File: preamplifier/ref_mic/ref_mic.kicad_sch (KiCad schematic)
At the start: 28 parts, among them J1 XLR3, U1 OPA1611

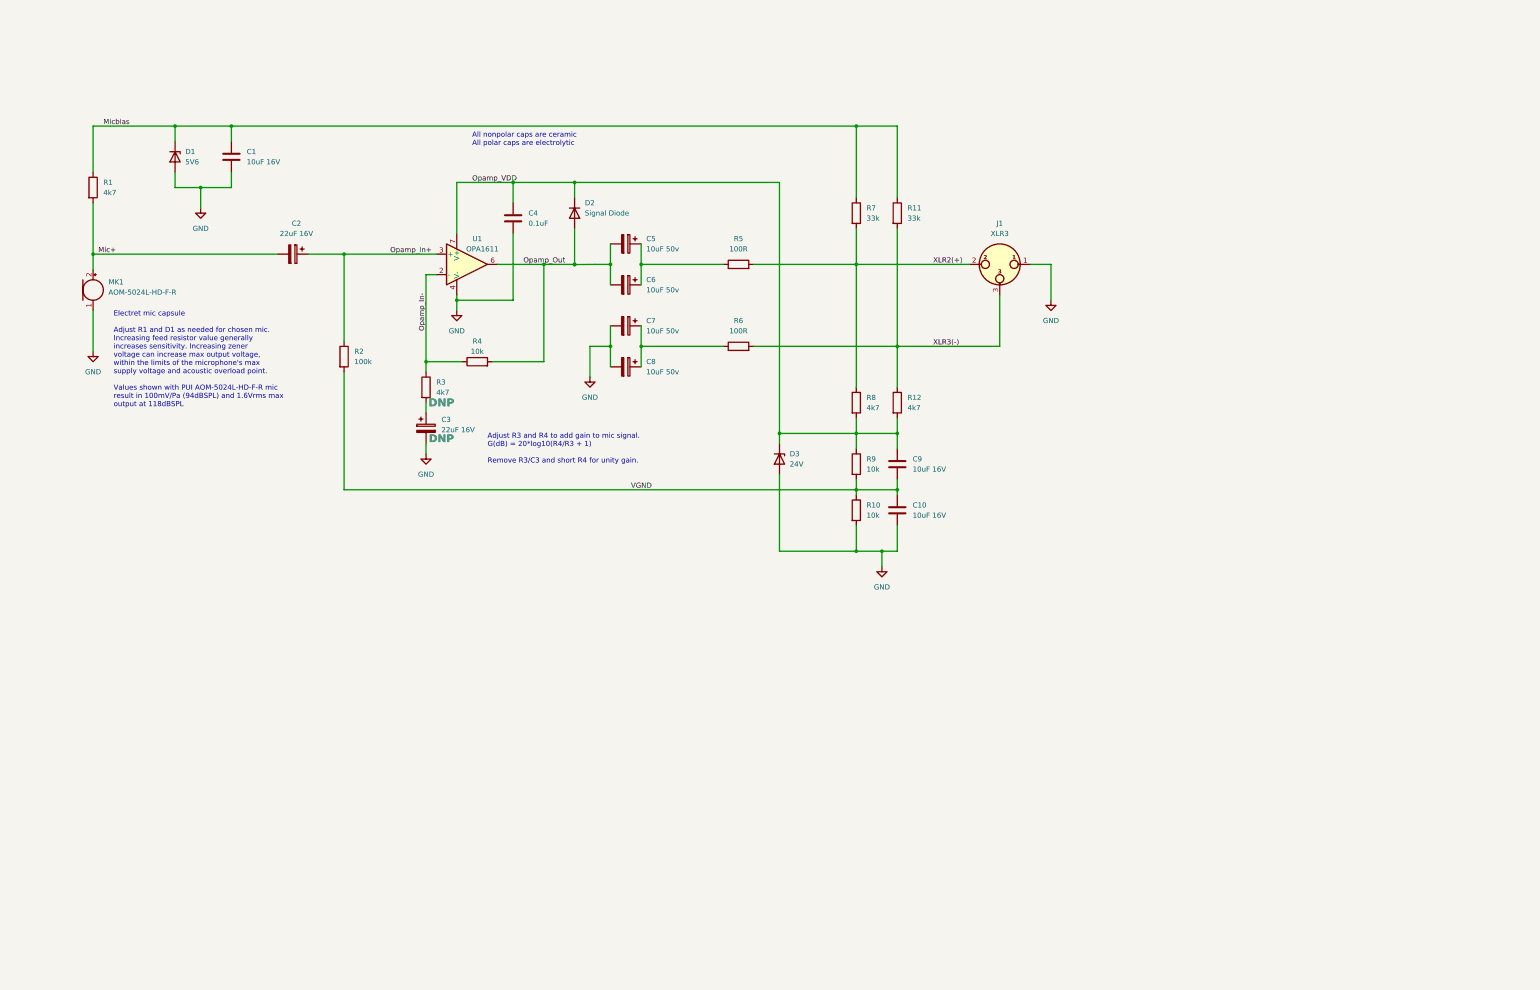
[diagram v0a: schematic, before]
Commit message: Initial v2 schematic, including high frequency correction filter for specified mic, library for slide switch. Update project to KiCAD 9.0 and change DNPs to use built in DNP feature.
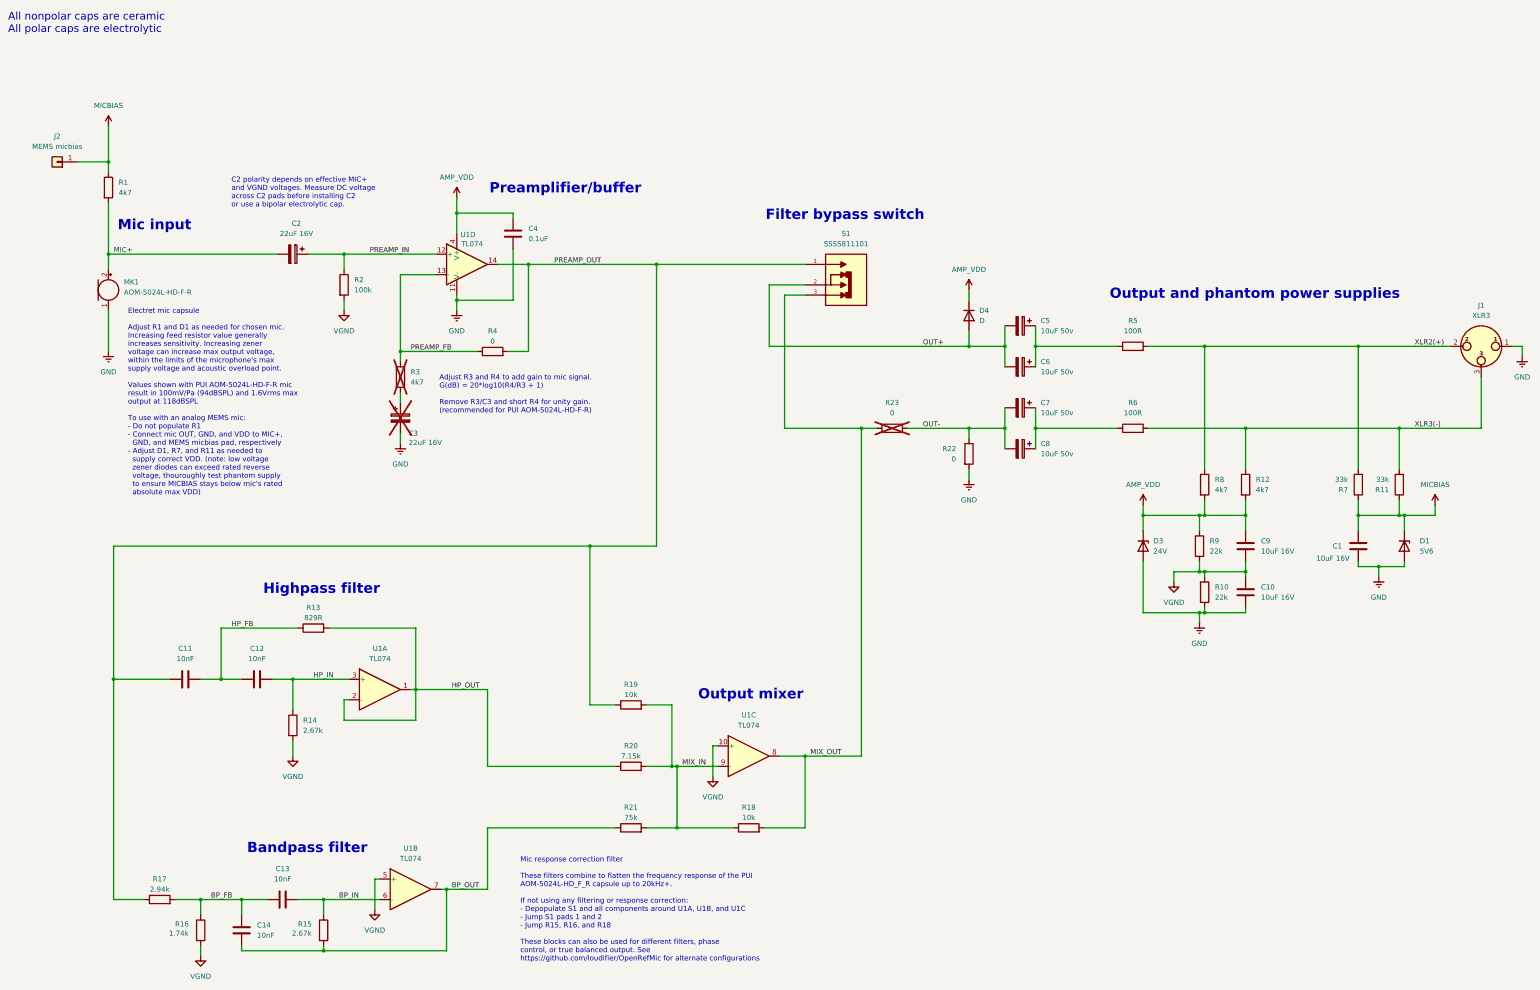
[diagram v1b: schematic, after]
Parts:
- removed D2: Signal Diode, Package_TO_SOT_SMD:SOT-23_Handsoldering, symbol Simulation_SPICE:DIODE
- removed U1: OPA1611, Package_SO:SOIC-8_3.9x4.9mm_P1.27mm, symbol Simulation_SPICE:OPAMP
- added C11, C12, C13, C14: 10nF, Capacitor_SMD:C_0805_2012Metric_Pad1.18x1.45mm_HandSolder, symbol Device:C
- added D4: D, symbol Device:D
- added J2: MEMS micbias, symbol Connector_Generic:Conn_01x01
- added R13: 829R, Resistor_SMD:R_0603_1608Metric_Pad0.98x0.95mm_HandSolder, symbol Device:R
- added R14, R15: 2.67k, Resistor_SMD:R_0603_1608Metric_Pad0.98x0.95mm_HandSolder, symbol Device:R
- added R16: 1.74k, Resistor_SMD:R_0603_1608Metric_Pad0.98x0.95mm_HandSolder, symbol Device:R
- added R17: 2.94k, Resistor_SMD:R_0603_1608Metric_Pad0.98x0.95mm_HandSolder, symbol Device:R
- added R18, R19: 10k, Resistor_SMD:R_0603_1608Metric_Pad0.98x0.95mm_HandSolder, symbol Device:R
- added R20: 7.15k, Resistor_SMD:R_0603_1608Metric_Pad0.98x0.95mm_HandSolder, symbol Device:R
- added R21: 75k, Resistor_SMD:R_0603_1608Metric_Pad0.98x0.95mm_HandSolder, symbol Device:R
- added R22, R23: 0, Resistor_SMD:R_0603_1608Metric_Pad0.98x0.95mm_HandSolder, symbol Device:R
- added S1: SSSS811101, SSSS811101:SW_SSSS811101, symbol SSSS811101:SSSS811101
- added U1, U2: TL074, symbol Amplifier_Operational:TL074
- C3, R3: DNP DNP -> (none); now not fitted
- R10, R9: value 10k -> 22k
- R4: value 10k -> 0
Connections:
- net GND: now also R22.2, U2.11 (V-); no longer C7.2, C8.2
- net VGND: now also R14.2, R16.2, U1.10 (+), U1.5 (+)
- net Mic+ renamed MIC+
- net Micbias renamed MICBIAS
- net MICBIAS: now also J2.1 (Pin_1)
- net Opamp_In+ renamed PREAMP_IN
- net PREAMP_IN: now also U1.12 (+)
- net Opamp_In- renamed PREAMP_FB
- net PREAMP_FB: now also U1.13 (-)
- net Opamp_Out renamed OUT+
- net OUT+: now also D4.2 (A), S1.2; no longer R4.2
- net Opamp_VDD renamed AMP_VDD
- net AMP_VDD: now also D4.1 (K), U2.4 (V+)
- new net BP_FB: C13.1, C14.2, R16.1, R17.2
- new net BP_IN: C13.2, R15.1, U1.6 (-)
- new net BP_OUT: C14.1, R15.2, R21.1, U1.7
- new net HP_FB: C11.2, C12.1, R13.1
- new net HP_IN: C12.2, R14.1, U1.3 (+)
- new net HP_OUT: R13.2, R20.1, U1.1, U1.2 (-)
- new net MIX_IN: R18.1, R19.2, R20.2, R21.2, U1.9 (-)
- new net MIX_OUT: R18.2, R23.1, S1.3, U1.8
- new net OUT-: C7.2, C8.2, R22.1, R23.2
- new net PREAMP_OUT: C11.1, R17.1, R19.1, R4.2, S1.1, U1.14
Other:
- note added: "Adjust R3 and R4 to add gain to mic signal. G(dB) = 20*log10(R4/R3 + 1) Remove R3/C3 and short R4 for unity gain. (recommended for PUI AOM-5024L-HD-F-R)"
- note added: "Bandpass filter"
- note added: "C2 polarity depends on effective MIC+ and VGND voltages. Measure DC voltage across C2 pads before installing C2 or use a bipolar electrolytic cap."
- note added: "Electret mic capsule Adjust R1 and D1 as needed for chosen mic. Increasing feed resistor value generally increases sensitivity. Increasing zener voltage can increase max output voltage, within the limits of the microphone's max supply voltage and acoustic overload point. Values shown with PUI AOM-5024L-HD-F-R mic result in 100mV/Pa (94dBSPL) and 1.6Vrms max output at 118dBSPL To use with an analo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"
- note added: "Filter bypass switch"
- note added: "Highpass filter"
- note added: "Mic input"
- note added: "Mic response correction filter These filters combine to flatten the frequency response of the PUI AOM-5024L-HD_F_R capsule up to 20kHz+. If not using any filtering or response correction: - Depopulate S1 and all components around U1A, U1B, and U1C - Jump S1 pads 1 and 2 - Jump R15, R16, and R18 These blocks can also be used for different filters, phase control, or true balanced output. See https: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"
- note added: "Output and phantom power supplies"
- note added: "Output mixer"
- note added: "Preamplifier/buffer"
- note removed: "Adjust R3 and R4 to add gain to mic signal. G(dB) = 20*log10(R4/R3 + 1) Remove R3/C3 and short R4 for unity gain."
- note removed: "Electret mic capsule Adjust R1 and D1 as needed for chosen mic. Increasing feed resistor value generally increases sensitivity. Increasing zener voltage can increase max output voltage, within the limits of the microphone's max supply voltage and acoustic overload point. Values shown with PUI AOM-5024L-HD-F-R mic result in 100mV/Pa (94dBSPL) and 1.6Vrms max output at 118dBSPL"
- moved on the sheet: C1, C10, C4, C5, C6, C7, C8, C9, D1, D3, J1, MK1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

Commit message: Bulk of v2 updates, before assembly and testing new design - KiCAD project - gerber outputs - schematic PDF - mechanical design (Fusion project, STEP assembly, STL outputs)
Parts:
- removed C6, C8: 10uF 50v, Capacitor_SMD:CP_Elec_6.3x5.4_Nichicon, symbol Device:C_Polarized
- added C1: 4.7uF 35V, Capacitor_SMD:CP_Elec_4x4.5, symbol Device:C_Polarized
- C10: renamed from C7; footprint Capacitor_SMD:CP_Elec_6.3x5.4_Nichicon -> Capacitor_SMD:CP_Elec_6.3x4.5; DigiKey_Part_Number (none) -> UZG1H100MCL1GB; LCSC_Part_Number (none) -> Honor Elec GVS1H100M0604
- C11: renamed from C9; footprint Capacitor_SMD:C_0805_2012Metric_Pad1.18x1.45mm_HandSolder -> Capacitor_SMD:C_1206_3216Metric; DigiKey_Part_Number (none) -> CL31B106KOHNNNE; LCSC_Part_Number (none) -> Samsung Electro-Mechanics CL31B106KOHNNNE; Size (none) -> 1206
- C12: renamed from C10; footprint Capacitor_SMD:C_0805_2012Metric_Pad1.18x1.45mm_HandSolder -> Capacitor_SMD:C_1206_3216Metric; DigiKey_Part_Number (none) -> CL31B106KOHNNNE; LCSC_Part_Number (none) -> Samsung Electro-Mechanics CL31B106KOHNNNE
- C13: renamed from C1; footprint Capacitor_SMD:C_0805_2012Metric_Pad1.18x1.45mm_HandSolder -> Capacitor_SMD:C_1206_3216Metric; DigiKey_Part_Number (none) -> CL31B106KOHNNNE; LCSC_Part_Number (none) -> Samsung Electro-Mechanics CL31B106KOHNNNE
- C2: value 22uF 16V -> 4.7uF 35V; footprint Capacitor_SMD:CP_Elec_5x5.4 -> Capacitor_SMD:CP_Elec_4x4.5; DigiKey_Part_Number (none) -> UZR1V4R7MCL1GB; LCSC_Part_Number (none) -> Lelon VSS100M1CTR-0404
- C3: renamed from C11; footprint Capacitor_SMD:C_0805_2012Metric_Pad1.18x1.45mm_HandSolder -> Capacitor_SMD:C_0402_1005Metric; DigiKey_Part_Number (none) -> CC0402KRX7R9BB103; LCSC_Part_Number (none) -> YAGEO CC0402KRX7R9BB103
- C4: renamed from C12; footprint Capacitor_SMD:C_0805_2012Metric_Pad1.18x1.45mm_HandSolder -> Capacitor_SMD:C_0402_1005Metric; DigiKey_Part_Number (none) -> CC0402KRX7R9BB103; LCSC_Part_Number (none) -> YAGEO CC0402KRX7R9BB103
- C5: renamed from C14; footprint Capacitor_SMD:C_0805_2012Metric_Pad1.18x1.45mm_HandSolder -> Capacitor_SMD:C_0402_1005Metric; DigiKey_Part_Number (none) -> CC0402KRX7R9BB103; LCSC_Part_Number (none) -> YAGEO CC0402KRX7R9BB103
- C6: renamed from C13; footprint Capacitor_SMD:C_0805_2012Metric_Pad1.18x1.45mm_HandSolder -> Capacitor_SMD:C_0402_1005Metric; DigiKey_Part_Number (none) -> CC0402KRX7R9BB103; LCSC_Part_Number (none) -> YAGEO CC0402KRX7R9BB103
- C7: renamed from C3; value 22uF 16V -> 10uF 16V; footprint Capacitor_SMD:CP_Elec_5x5.4 -> Capacitor_SMD:CP_Elec_4x4.5; DigiKey_Part_Number (none) -> UZG1C100MCL1GB; LCSC_Part_Number (none) -> Lelon VSS100M1CTR-0404; now in the parts list
- C8: renamed from C4; footprint Capacitor_SMD:C_0603_1608Metric_Pad1.08x0.95mm_HandSolder -> Capacitor_SMD:C_0402_1005Metric; DigiKey_Part_Number (none) -> CC0402KRX5R9BB104; LCSC_Part_Number (none) -> YAGEO CC0402KRX5R9BB104
- C9: renamed from C5; footprint Capacitor_SMD:CP_Elec_6.3x5.4_Nichicon -> Capacitor_SMD:CP_Elec_6.3x4.5; DigiKey_Part_Number (none) -> UZG1H100MCL1GB; LCSC_Part_Number (none) -> Honor Elec GVS1H100M0604
- D1: renamed from D4; value D -> 1N4148; footprint (none) -> Diode_SMD:D_SOD-523; DigiKey_Part_Number (none) -> 1N4148X-TP; LCSC_Part_Number (none) -> MCC 1N4148X-TP
- D2: renamed from D3; footprint Package_TO_SOT_SMD:SOT-23_Handsoldering -> Diode_SMD:D_SOD-523; DigiKey_Part_Number (none) -> BZT585B24T-7; LCSC_Part_Number (none) -> Diodes Incorporated BZT585B24T-7
- D3: renamed from D1; footprint Package_TO_SOT_SMD:SC-59_Handsoldering -> Diode_SMD:D_SOD-523; DigiKey_Part_Number (none) -> BZT52C5V6T-7; LCSC_Part_Number (none) -> Diodes Incorporated BZT52C5V6T-7
- J1: renamed from J2; footprint (none) -> Connector_PinHeader_2.54mm:PinHeader_1x01_P2.54mm_Vertical; now left out of the parts list
- J2: renamed from J1; value XLR3 -> Mini XLR Male; footprint Connector_PinHeader_2.54mm:PinHeader_1x03_P2.54mm_Vertical -> OpenRefMic:Switchcraft_T3BM_edgemount; DigiKey_Part_Number (none) -> TB3M; LCSC_Part_Number (none) -> Switchcraft TB3M (not normally stocked)
- MK1: footprint Connector_PinHeader_2.54mm:PinHeader_1x02_P2.54mm_Vertical -> Connector_PinSocket_2.54mm:PinSocket_1x02_P2.54mm_Horizontal; DigiKey_Part_Number (none) -> AOM-5024L-HD-F-R; LCSC_Part_Number (none) -> PUI Audio, Inc. AOM-5024L-HD-F-R (not normally stocked)
- R1: footprint Resistor_SMD:R_0603_1608Metric_Pad0.98x0.95mm_HandSolder -> Resistor_SMD:R_0402_1005Metric; DigiKey_Part_Number (none) -> RC0402FR-074K7L; LCSC_Part_Number (none) -> YAGEO RC0402FR-074K7L
- R10: renamed from R19; footprint Resistor_SMD:R_0603_1608Metric_Pad0.98x0.95mm_HandSolder -> Resistor_SMD:R_0402_1005Metric; DigiKey_Part_Number (none) -> RC0402FR-0710KL; LCSC_Part_Number (none) -> YAGEO RC0402FR-0710KL
- R11: renamed from R20; footprint Resistor_SMD:R_0603_1608Metric_Pad0.98x0.95mm_HandSolder -> Resistor_SMD:R_0402_1005Metric; DigiKey_Part_Number (none) -> RC0402FR-077K15L; LCSC_Part_Number (none) -> YAGEO RC0402FR-077K15L
- R12: renamed from R21; footprint Resistor_SMD:R_0603_1608Metric_Pad0.98x0.95mm_HandSolder -> Resistor_SMD:R_0402_1005Metric; DigiKey_Part_Number (none) -> RC0402FR-1375KL; LCSC_Part_Number (none) -> YAGEO RC0402FR-1375KL
- R13: renamed from R18; footprint Resistor_SMD:R_0603_1608Metric_Pad0.98x0.95mm_HandSolder -> Resistor_SMD:R_0402_1005Metric; DigiKey_Part_Number (none) -> RC0402FR-0710KL; LCSC_Part_Number (none) -> YAGEO RC0402FR-0710KL
- R14: renamed from R23; footprint Resistor_SMD:R_0603_1608Metric_Pad0.98x0.95mm_HandSolder -> Resistor_SMD:R_0402_1005Metric; DigiKey_Part_Number (none) -> RC0402JR-070RL; LCSC_Part_Number (none) -> YAGEO RC0402JR-070RL
- R15: renamed from R22; footprint Resistor_SMD:R_0603_1608Metric_Pad0.98x0.95mm_HandSolder -> Resistor_SMD:R_0402_1005Metric; DigiKey_Part_Number (none) -> RC0402JR-070RL; LCSC_Part_Number (none) -> YAGEO RC0402JR-070RL
- R16: renamed from R5; footprint Resistor_SMD:R_0603_1608Metric_Pad0.98x0.95mm_HandSolder -> Resistor_SMD:R_0402_1005Metric; DigiKey_Part_Number (none) -> RC0402FR-07100RL; LCSC_Part_Number (none) -> YAGEO RC0402FR-07100RL
- R17: renamed from R6; footprint Resistor_SMD:R_0603_1608Metric_Pad0.98x0.95mm_HandSolder -> Resistor_SMD:R_0402_1005Metric; DigiKey_Part_Number (none) -> RC0402FR-07100RL; LCSC_Part_Number (none) -> YAGEO RC0402FR-07100RL
- R18: renamed from R9; footprint Resistor_SMD:R_0603_1608Metric_Pad0.98x0.95mm_HandSolder -> Resistor_SMD:R_0402_1005Metric; DigiKey_Part_Number (none) -> RC0402FR-0722KL; LCSC_Part_Number (none) -> YAGEO RC0402FR-0722KL
- R19: renamed from R8; footprint Resistor_SMD:R_0603_1608Metric_Pad0.98x0.95mm_HandSolder -> Resistor_SMD:R_0402_1005Metric; DigiKey_Part_Number (none) -> RC0402FR-074K7L; LCSC_Part_Number (none) -> YAGEO RC0402FR-074K7L
- R2: renamed from R17; footprint Resistor_SMD:R_0603_1608Metric_Pad0.98x0.95mm_HandSolder -> Resistor_SMD:R_0402_1005Metric; DigiKey_Part_Number (none) -> RC0402FR-072K94L; LCSC_Part_Number (none) -> YAGEO RC0402FR-072K94L
- R20: renamed from R10; footprint Resistor_SMD:R_0603_1608Metric_Pad0.98x0.95mm_HandSolder -> Resistor_SMD:R_0402_1005Metric; DigiKey_Part_Number (none) -> RC0402FR-0722KL; LCSC_Part_Number (none) -> YAGEO RC0402FR-0722KL
- R21: renamed from R12; footprint Resistor_SMD:R_0603_1608Metric_Pad0.98x0.95mm_HandSolder -> Resistor_SMD:R_0402_1005Metric; DigiKey_Part_Number (none) -> RC0402FR-074K7L; LCSC_Part_Number (none) -> YAGEO RC0402FR-074K7L
- R22: renamed from R7; footprint Resistor_SMD:R_0603_1608Metric_Pad0.98x0.95mm_HandSolder -> Resistor_SMD:R_0402_1005Metric; DigiKey_Part_Number (none) -> RC0402FR-0733KL; LCSC_Part_Number (none) -> YAGEO RC0402FR-0733KL
- R23: renamed from R11; footprint Resistor_SMD:R_0603_1608Metric_Pad0.98x0.95mm_HandSolder -> Resistor_SMD:R_0402_1005Metric; DigiKey_Part_Number (none) -> RC0402FR-0733KL; LCSC_Part_Number (none) -> YAGEO RC0402FR-0733KL
- R3: renamed from R16; footprint Resistor_SMD:R_0603_1608Metric_Pad0.98x0.95mm_HandSolder -> Resistor_SMD:R_0402_1005Metric; DigiKey_Part_Number (none) -> RC0402FR-071K74L; LCSC_Part_Number (none) -> YAGEO RC0402FR-071K74L
- R4: renamed from R14; footprint Resistor_SMD:R_0603_1608Metric_Pad0.98x0.95mm_HandSolder -> Resistor_SMD:R_0402_1005Metric; DigiKey_Part_Number (none) -> RC0402FR-072K67L; LCSC_Part_Number (none) -> YAGEO RC0402FR-072K67L
- R5: renamed from R13; value 829R -> 825R; footprint Resistor_SMD:R_0603_1608Metric_Pad0.98x0.95mm_HandSolder -> Resistor_SMD:R_0402_1005Metric; DigiKey_Part_Number (none) -> RC0402FR-07825RL; LCSC_Part_Number (none) -> YAGEO RC0402FR-07825RL
- R6: renamed from R15; footprint Resistor_SMD:R_0603_1608Metric_Pad0.98x0.95mm_HandSolder -> Resistor_SMD:R_0402_1005Metric; DigiKey_Part_Number (none) -> RC0402FR-072K67L; LCSC_Part_Number (none) -> YAGEO RC0402FR-072K67L
- R7: renamed from R2; footprint Resistor_SMD:R_0603_1608Metric_Pad0.98x0.95mm_HandSolder -> Resistor_SMD:R_0402_1005Metric; DigiKey_Part_Number (none) -> RC0402FR-07100KL; LCSC_Part_Number (none) -> YAGEO RC0402FR-07100KL
- R8: renamed from R3; footprint Resistor_SMD:R_0603_1608Metric_Pad0.98x0.95mm_HandSolder -> Resistor_SMD:R_0402_1005Metric; DigiKey_Part_Number (none) -> RC0402FR-074K7L; LCSC_Part_Number (none) -> YAGEO RC0402FR-074K7L; now in the parts list
- R9: renamed from R4; footprint Resistor_SMD:R_0603_1608Metric_Pad0.98x0.95mm_HandSolder -> Resistor_SMD:R_0402_1005Metric; DigiKey_Part_Number (none) -> RC0402JR-070RL; LCSC_Part_Number (none) -> YAGEO RC0402JR-070RL
- S1: value SSSS811101 -> CL-SB-12B-01T; footprint SSSS811101:SW_SSSS811101 -> OpenRefMic:CL-SB-12B-01_NDC; symbol SSSS811101:SSSS811101 -> Switch:SW_SPDT; Check_prices https://www.snapeda.com/parts/SSSS811101/ALPS/view-part/?re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 -> (none); Description_1 Switch Slide SP Side Slide 0.3A 5VDC 10000Cycles Gull Wing 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 -> (none); DigiKey_Part_Number 4809-SSSS811101TR-ND -> CL-SB-12B-01T; LCSC_Part_Number (none) -> Nidec CL-SB-12B-01T; MANUFACTURER ALPS -> (none); MAXIMUM_PACKAGE_HEIGHT 1.60 mm -> (none); MF ALPS -> (none); MP SSSS811101 -> (none); PARTREV N/A -> (none); Package None -> (none); STANDARD Manufacturer Recommendations -> (none); SnapEDA_Link https://www.snapeda.com/parts/SSSS811101/ALPS/view-part/?re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 -> (none)
- U1: renamed from U2; value TL074 -> OPA1664; footprint (none) -> Package_SO:SO-14_3.9x8.65mm_P1.27mm; DigiKey_Part_Number (none) -> OPA1664AIDR; LCSC_Part_Number (none) -> TI OPA1664AID
- U1: value TL074 -> OPA1664; footprint (none) -> Package_SO:SO-14_3.9x8.65mm_P1.27mm; DigiKey_Part_Number (none) -> OPA1664AIDR; LCSC_Part_Number (none) -> TI OPA1664AID
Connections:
- net AMP_VDD: now also D2.1 (K); no longer D2.3 (K)
- net GND: now also D2.2 (A), D3.2 (A); no longer D2.1 (A), D3.1 (A)
- net MIC+: now also C1.2; no longer C2.2
- net MICBIAS: now also D3.1 (K); no longer D3.3 (K)
- net PREAMP_IN: now also C2.2; no longer C2.1
- new net: C1.1, C2.1
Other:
- note added: "Adjust ${/9538e4ed-27e6-4c37-b989-9859dc0d49e8/b3fd72eb-3c48-4dba-b4ba-166366a55091:REFERENCE} and ${/9538e4ed-27e6-4c37-b989-9859dc0d49e8/bf293fc3-0f93-4cc4-ba29-ea566fa56ab7:REFERENCE} to add gain to mic signal. Gain(dB) = 20*log10(${/9538e4ed-27e6-4c37-b989-9859dc0d49e8/bf293fc3-0f93-4cc4-ba29-ea566fa56ab7:REFERENCE}/${/9538e4ed-27e6-4c37-b989-9859dc0d49e8/b3fd72eb-3c48-4dba-b4ba-166366a55091: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"
- note added: "Electret mic capsule Adjust ${/9538e4ed-27e6-4c37-b989-9859dc0d49e8/e271bef5-15e4-40c9-876c-89aee48ff184:REFERENCE} and ${/9538e4ed-27e6-4c37-b989-9859dc0d49e8/d3f055ef-f3d2-49ea-a4d1-c26857ed3592:REFERENCE} as needed for chosen mic. Increasing feed resistor value generally increases sensitivity. Increasing zener voltage can increase max output voltage, within the limits of the microphone's max s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"
- note added: "Filter mixer"
- note added: "Mic response correction filter These filters combine to flatten the frequency response of the PUI AOM-5024L-HD_F_R capsule up to 20kHz+. If not using any filtering or response correction: - Depopulate ${/9538e4ed-27e6-4c37-b989-9859dc0d49e8/5f610e3d-6d12-430c-b922-2699dde64c64:REFERENCE} and all components around ${/9538e4ed-27e6-4c37-b989-9859dc0d49e8/b6755635-a29e-499f-87f5-7eb5ed143b34:REFEREN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"
- note added: "Output and phantom power"
- note removed: "Adjust R3 and R4 to add gain to mic signal. G(dB) = 20*log10(R4/R3 + 1) Remove R3/C3 and short R4 for unity gain. (recommended for PUI AOM-5024L-HD-F-R)"
- note removed: "C2 polarity depends on effective MIC+ and VGND voltages. Measure DC voltage across C2 pads before installing C2 or use a bipolar electrolytic cap."
- note removed: "Electret mic capsule Adjust R1 and D1 as needed for chosen mic. Increasing feed resistor value generally increases sensitivity. Increasing zener voltage can increase max output voltage, within the limits of the microphone's max supply voltage and acoustic overload point. Values shown with PUI AOM-5024L-HD-F-R mic result in 100mV/Pa (94dBSPL) and 1.6Vrms max output at 118dBSPL To use with an analo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"
- note removed: "Mic response correction filter These filters combine to flatten the frequency response of the PUI AOM-5024L-HD_F_R capsule up to 20kHz+. If not using any filtering or response correction: - Depopulate S1 and all components around U1A, U1B, and U1C - Jump S1 pads 1 and 2 - Jump R15, R16, and R18 These blocks can also be used for different filters, phase control, or true balanced output. See https: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"
- note removed: "Output and phantom power supplies"
- note removed: "Output mixer"
- moved on the sheet: C10, C11, C12, C13, C9, D1, D2, D3, J2, R10, R11, R12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
